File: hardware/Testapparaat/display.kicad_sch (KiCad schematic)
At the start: 4 parts

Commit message: -enh Made the schematic for the main unit almost complete :)
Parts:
- gave numbers to parts that had none: 4
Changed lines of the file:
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@@
   (symbol (lib_id "power:GND") (at 59.69 109.22 0) (unit 1)
     (in_bom yes) (on_board yes) (fields_autoplaced)
-    (property "Reference" "#PWR?" (id 0) (at 59.69 115.57 0)
+    (property "Reference" "#PWR034" (id 0) (at 59.69 115.57 0)
       (effects (font (size 1.27 1.27)) hide)
     )
@@
   (symbol (lib_id "power:GND") (at 60.325 48.26 0) (unit 1)
     (in_bom yes) (on_board yes) (fields_autoplaced)
-    (property "Reference" "#PWR?" (id 0) (at 60.325 54.61 0)
+    (property "Reference" "#PWR035" (id 0) (at 60.325 54.61 0)
       (effects (font (size 1.27 1.27)) hide)
     )
@@
   (symbol (lib_id "power:+3.3V") (at 49.53 104.14 270) (unit 1)
     (in_bom yes) (on_board yes) (fields_autoplaced)
-    (property "Reference" "#PWR?" (id 0) (at 45.72 104.14 0)
+    (property "Reference" "#PWR031" (id 0) (at 45.72 104.14 0)
       (effects (font (size 1.27 1.27)) hide)
     )
@@
   (symbol (lib_id "Connector:Conn_01x40_Male") (at 42.545 71.12 0) (unit 1)
     (in_bom yes) (on_board yes) (fields_autoplaced)
-    (property "Reference" "J?" (id 0) (at 43.18 17.78 0))
+    (property "Reference" "J5" (id 0) (at 43.18 17.78 0))
     (property "Value" "FPC_40P_LCD_ILI9488" (id 1) (at 43.18 20.32 0))
     (property "Footprint" "" (id 2) (at 42.545 71.12 0)
@@
   (symbol (lib_id "power:GND") (at 47.625 121.92 0) (unit 1)
     (in_bom yes) (on_board yes) (fields_autoplaced)
-    (property "Reference" "#PWR?" (id 0) (at 47.625 128.27 0)
+    (property "Reference" "#PWR030" (id 0) (at 47.625 128.27 0)
       (effects (font (size 1.27 1.27)) hide)
     )
@@
   (symbol (lib_id "power:GND") (at 53.34 27.94 0) (unit 1)
     (in_bom yes) (on_board yes) (fields_autoplaced)
-    (property "Reference" "#PWR?" (id 0) (at 53.34 34.29 0)
+    (property "Reference" "#PWR033" (id 0) (at 53.34 34.29 0)
       (effects (font (size 1.27 1.27)) hide)
     )
@@
   (symbol (lib_id "power:+3.3V") (at 47.625 36.83 270) (unit 1)
     (in_bom yes) (on_board yes) (fields_autoplaced)
-    (property "Reference" "#PWR?" (id 0) (at 43.815 36.83 0)
+    (property "Reference" "#PWR029" (id 0) (at 43.815 36.83 0)
       (effects (font (size 1.27 1.27)) hide)
     )
@@
   (symbol (lib_id "power:GND") (at 50.8 81.915 0) (unit 1)
     (in_bom yes) (on_board yes) (fields_autoplaced)
-    (property "Reference" "#PWR?" (id 0) (at 50.8 88.265 0)
+    (property "Reference" "#PWR032" (id 0) (at 50.8 88.265 0)
       (effects (font (size 1.27 1.27)) hide)
     )
@@
   (symbol (lib_id "Device:R") (at 51.435 111.76 90) (unit 1)
     (in_bom yes) (on_board yes)
-    (property "Reference" "R?" (id 0) (at 55.245 113.03 90))
+    (property "Reference" "R13" (id 0) (at 55.245 113.03 90))
     (property "Value" "220" (id 1) (at 51.435 111.76 90))
     (property "Footprint" "" (id 2) (at 51.435 113.538 90)
@@
   (symbol (lib_id "Device:R") (at 51.435 106.68 90) (unit 1)
     (in_bom yes) (on_board yes)
-    (property "Reference" "R?" (id 0) (at 55.245 107.95 90))
+    (property "Reference" "R11" (id 0) (at 55.245 107.95 90))
     (property "Value" "220" (id 1) (at 51.435 106.68 90))
     (property "Footprint" "" (id 2) (at 51.435 108.458 90)
@@
   (symbol (lib_id "Device:R") (at 51.435 109.22 90) (unit 1)
     (in_bom yes) (on_board yes)
-    (property "Reference" "R?" (id 0) (at 55.245 110.49 90))
+    (property "Reference" "R12" (id 0) (at 55.245 110.49 90))
     (property "Value" "220" (id 1) (at 51.435 109.22 90))
     (property "Footprint" "" (id 2) (at 51.435 110.998 90)

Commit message: -enh made some changes to schematic and assigned fp
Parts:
- J5: footprint (none) -> Connector_FFC-FPC:TE_4-1734839-0_1x40-1MP_P0.5mm_Horizontal
- R11, R12, R13: footprint (none) -> Resistor_SMD:R_0603_1608Metric_Pad0.98x0.95mm_HandSolder
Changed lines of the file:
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@@
     (property "Reference" "J5" (id 0) (at 43.18 17.78 0))
     (property "Value" "FPC_40P_LCD_ILI9488" (id 1) (at 43.18 20.32 0))
-    (property "Footprint" "" (id 2) (at 42.545 71.12 0)
+    (property "Footprint" "Connector_FFC-FPC:TE_4-1734839-0_1x40-1MP_P0.5mm_Horizontal" (id 2) (at 42.545 71.12 0)
       (effects (font (size 1.27 1.27)) hide)
     )
@@
     (property "Reference" "R13" (id 0) (at 55.245 113.03 90))
     (property "Value" "220" (id 1) (at 51.435 111.76 90))
-    (property "Footprint" "" (id 2) (at 51.435 113.538 90)
+    (property "Footprint" "Resistor_SMD:R_0603_1608Metric_Pad0.98x0.95mm_HandSolder" (id 2) (at 51.435 113.538 90)
       (effects (font (size 1.27 1.27)) hide)
     )
@@
     (property "Reference" "R11" (id 0) (at 55.245 107.95 90))
     (property "Value" "220" (id 1) (at 51.435 106.68 90))
-    (property "Footprint" "" (id 2) (at 51.435 108.458 90)
+    (property "Footprint" "Resistor_SMD:R_0603_1608Metric_Pad0.98x0.95mm_HandSolder" (id 2) (at 51.435 108.458 90)
       (effects (font (size 1.27 1.27)) hide)
     )
@@
     (property "Reference" "R12" (id 0) (at 55.245 110.49 90))
     (property "Value" "220" (id 1) (at 51.435 109.22 90))
-    (property "Footprint" "" (id 2) (at 51.435 110.998 90)
+    (property "Footprint" "Resistor_SMD:R_0603_1608Metric_Pad0.98x0.95mm_HandSolder" (id 2) (at 51.435 110.998 90)
       (effects (font (size 1.27 1.27)) hide)
     )

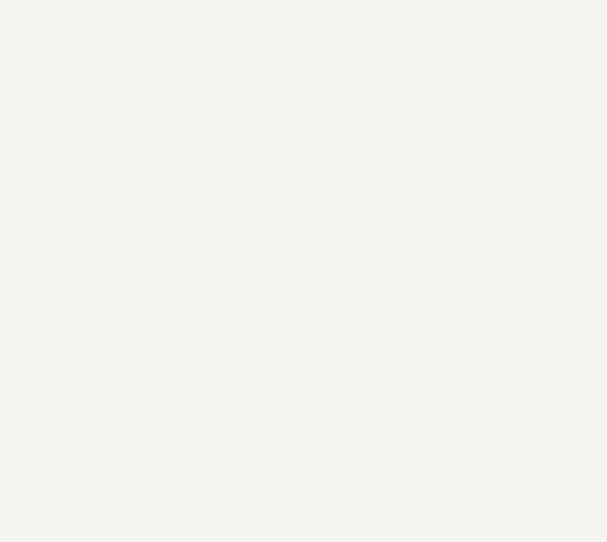
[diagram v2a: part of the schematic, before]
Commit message: -enh add seperate schematic and pcb for io ports/slots
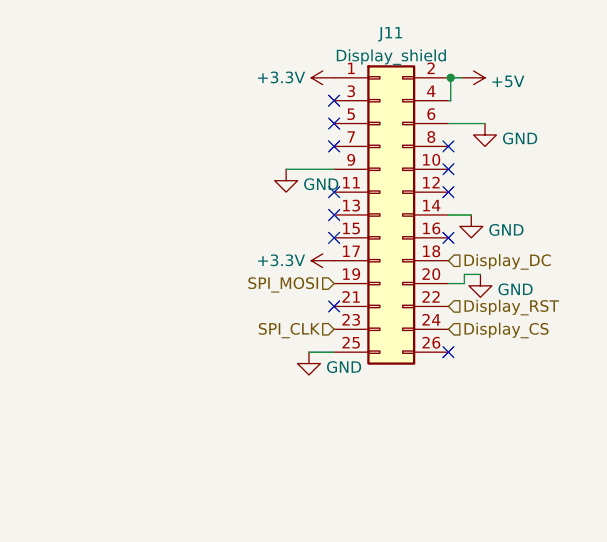
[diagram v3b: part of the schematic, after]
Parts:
- added J11: Display_shield, Connector_PinHeader_2.54mm:PinHeader_2x13_P2.54mm_Vertical_SMD, symbol Connector_Generic:Conn_02x13_Odd_Even
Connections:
- net +3.3V: now also J11.1 (Pin_1), J11.17 (Pin_17)
- net Display_CS: now also J11.24 (Pin_24)
- net Display_DC: now also J11.18 (Pin_18)
- net Display_RST: now also J11.22 (Pin_22)
- net GND: now also J11.14 (Pin_14), J11.20 (Pin_20), J11.25 (Pin_25), J11.6 (Pin_6), J11.9 (Pin_9)
- net SPI_CLK: now also J11.23 (Pin_23)
- net SPI_MOSI: now also J11.19 (Pin_19)
- new net +5V: J11.2 (Pin_2), J11.4 (Pin_4)
- no-connect marks 6 -> 18

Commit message: -add BOM
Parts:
- added C18, C19, C20, C22: 100n, Capacitor_SMD:C_0603_1608Metric_Pad1.08x0.95mm_HandSolder, symbol Device:C_Small
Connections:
- net +3.3V: now also C18.2, C19.2, C20.1
- net +5V: now also C22.1
- net GND: now also C18.1, C19.1, C20.2, C22.2

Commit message: -enh Made a start at pcb design
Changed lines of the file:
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@@
-    (pin "1")
-  )
-  (symbol (lib_id "power:+3.3V") (at 65.278 104.14 270) (unit 1)
-    (in_bom yes) (on_board yes) (fields_autoplaced)
-    (property "Reference" "#PWR031" (id 0) (at 61.468 104.14 0)
-      (effects (font (size 1.27 1.27)) hide)
-    )
-    (property "Value" "+3.3V" (id 1) (at 69.088 104.1399 90)
-      (effects (font (size 1.27 1.27)) (justify left))
-    )
-    (property "Footprint" "" (id 2) (at 65.278 104.14 0)
-      (effects (font (size 1.27 1.27)) hide)
-    )
-    (property "Datasheet" "" (id 3) (at 65.278 104.14 0)
-      (effects (font (size 1.27 1.27)) hide)
-    )
     (pin "1")
   )
@@
     (pin "9")
   )
+  (symbol (lib_id "power:+3.3V") (at 112.014 23.114 0) (unit 1)
+    (in_bom yes) (on_board yes)
+    (property "Reference" "#PWR099" (id 0) (at 112.014 26.924 0)
+      (effects (font (size 1.27 1.27)) hide)
+    )
+    (property "Value" "+3.3V" (id 1) (at 112.014 19.304 0))
+    (property "Footprint" "" (id 2) (at 112.014 23.114 0)
+      (effects (font (size 1.27 1.27)) hide)
+    )
+    (property "Datasheet" "" (id 3) (at 112.014 23.114 0)
+      (effects (font (size 1.27 1.27)) hide)
+    )
+    (pin "1")
+  )
   (symbol (lib_id "power:GND") (at 47.625 121.92 0) (unit 1)
     (in_bom yes) (on_board yes) (fields_autoplaced)
@@
     )
     (property "Datasheet" "" (id 3) (at 53.34 27.94 0)
-      (effects (font (size 1.27 1.27)) hide)
-    )
-    (pin "1")
-  )
-  (symbol (lib_id "power:+3.3V") (at 112.014 23.114 90) (unit 1)
-    (in_bom yes) (on_board yes)
-    (property "Reference" "#PWR083" (id 0) (at 115.824 23.114 0)
-      (effects (font (size 1.27 1.27)) hide)
-    )
-    (property "Value" "+3.3V" (id 1) (at 103.378 23.114 90)
-      (effects (font (size 1.27 1.27)) (justify right))
-    )
-    (property "Footprint" "" (id 2) (at 112.014 23.114 0)
-      (effects (font (size 1.27 1.27)) hide)
-    )
-    (property "Datasheet" "" (id 3) (at 112.014 23.114 0)
       (effects (font (size 1.27 1.27)) hide)
     )
@@
       (effects (font (size 1.27 1.27)) hide)
     )
+    (pin "1")
+  )
+  (symbol (lib_id "power:+3.3V") (at 65.278 104.14 0) (unit 1)
+    (in_bom yes) (on_board yes)
+    (property "Reference" "#PWR098" (id 0) (at 65.278 107.95 0)
+      (effects (font (size 1.27 1.27)) hide)
+    )
+    (property "Value" "+3.3V" (id 1) (at 65.278 100.33 0))
+    (property "Footprint" "" (id 2) (at 65.278 104.14 0)
+      (effects (font (size 1.27 1.27)) hide)
+    )
+    (property "Datasheet" "" (id 3) (at 65.278 104.14 0)
+      (effects (font (size 1.27 1.27)) hide)
+    )

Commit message: -add gerbers and minor improvements
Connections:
- net Display_TP_CS: now reaches J11.26 (Pin_26)
- no-connect marks 18 -> 17
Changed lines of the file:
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@@
   (no_connect (at 118.618 35.814))
   (no_connect (at 118.618 48.514))
-  (no_connect (at 131.318 53.594))
   (no_connect (at 47.625 55.88))
   (no_connect (at 47.625 40.64))
@@
   )
   (hierarchical_label "Display_CS" (shape input) (at 131.318 51.054 0)
+    (effects (font (size 1.27 1.27)) (justify left))
+  )
+  (hierarchical_label "Display_TP_CS" (shape input) (at 131.318 53.594 0)
     (effects (font (size 1.27 1.27)) (justify left))
   )
@@
   )
   (symbol (lib_id "power:GND") (at 113.284 33.274 0) (unit 1)
-    (in_bom yes) (on_board yes) (fields_autoplaced)
+    (in_bom yes) (on_board yes)
     (property "Reference" "#PWR081" (id 0) (at 113.284 39.624 0)
       (effects (font (size 1.27 1.27)) hide)
     )
-    (property "Value" "GND" (id 1) (at 115.189 34.9778 0)
-      (effects (font (size 1.27 1.27)) (justify left))
-    )
+    (property "Value" "GND" (id 1) (at 111.252 36.83 0)
+      (effects (font (size 1.27 1.27)) (justify left))
+    )

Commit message: -enh Final adjustments
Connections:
- net Display_TP_IRQ: now reaches J11.11 (Pin_11)
- net SPI_MISO: now reaches J11.21 (Pin_21)
- no-connect marks 17 -> 15
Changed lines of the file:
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@@
   (no_connect (at 131.318 35.814))
   (no_connect (at 131.318 40.894))
-  (no_connect (at 118.618 35.814))
-  (no_connect (at 118.618 48.514))
   (no_connect (at 47.625 55.88))
   (no_connect (at 47.625 40.64))
@@
     (effects (font (size 1.27 1.27)) (justify right))
   )
+  (hierarchical_label "Display_TP_IRQ" (shape input) (at 118.618 35.814 180)
+    (effects (font (size 1.27 1.27)) (justify right))
+  )
+  (hierarchical_label "SPI_MISO" (shape input) (at 118.618 48.514 180)
+    (effects (font (size 1.27 1.27)) (justify right))
+  )
